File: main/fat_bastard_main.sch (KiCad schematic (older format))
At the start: 58 parts, among them J1 INPUT, J2 TO LD 12V, J3 TO LD IN, J4 TO LD GAIN, J5 TO LD OUT, J6 12V IN, J7 DI OUT, J8 FOOTSW, J9 OUTPUT, K1 FINDER-30.22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

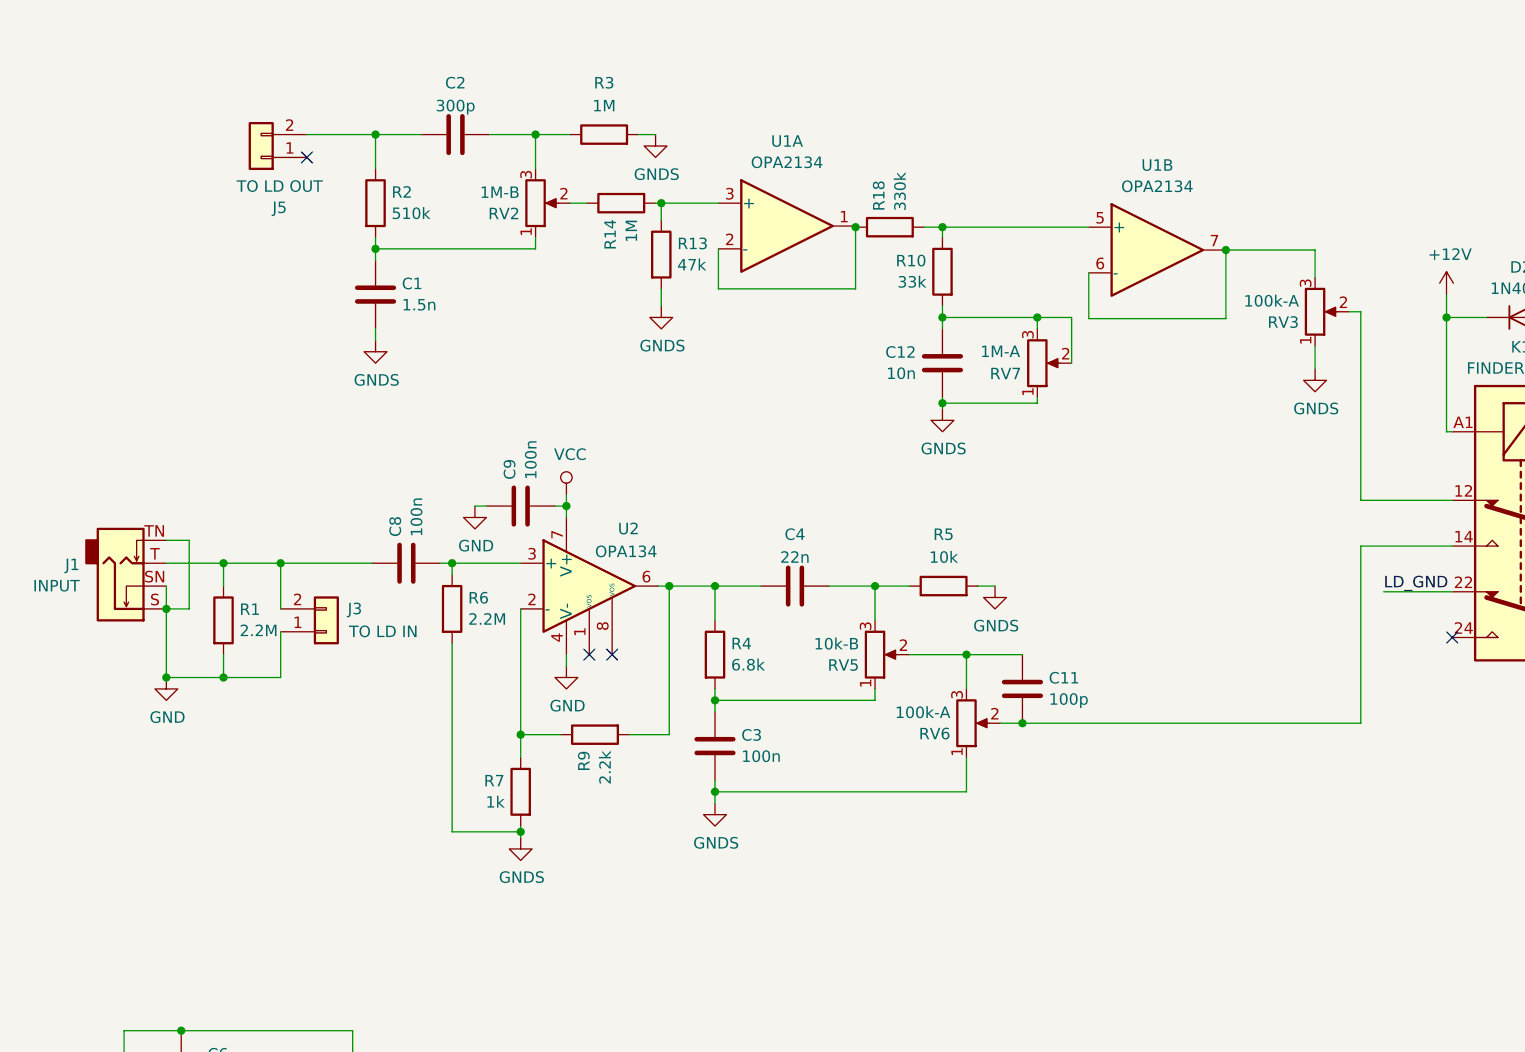
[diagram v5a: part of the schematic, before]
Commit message: [main] Fix channel switching
Due to changing the schematics layout in the previous version, default
channel is lead and is muted.

This commit restores the original layout and fixes the corresponding
traces.

Signed-off-by: Arnaud Ferraris <arnaud.ferraris@gmail.com>
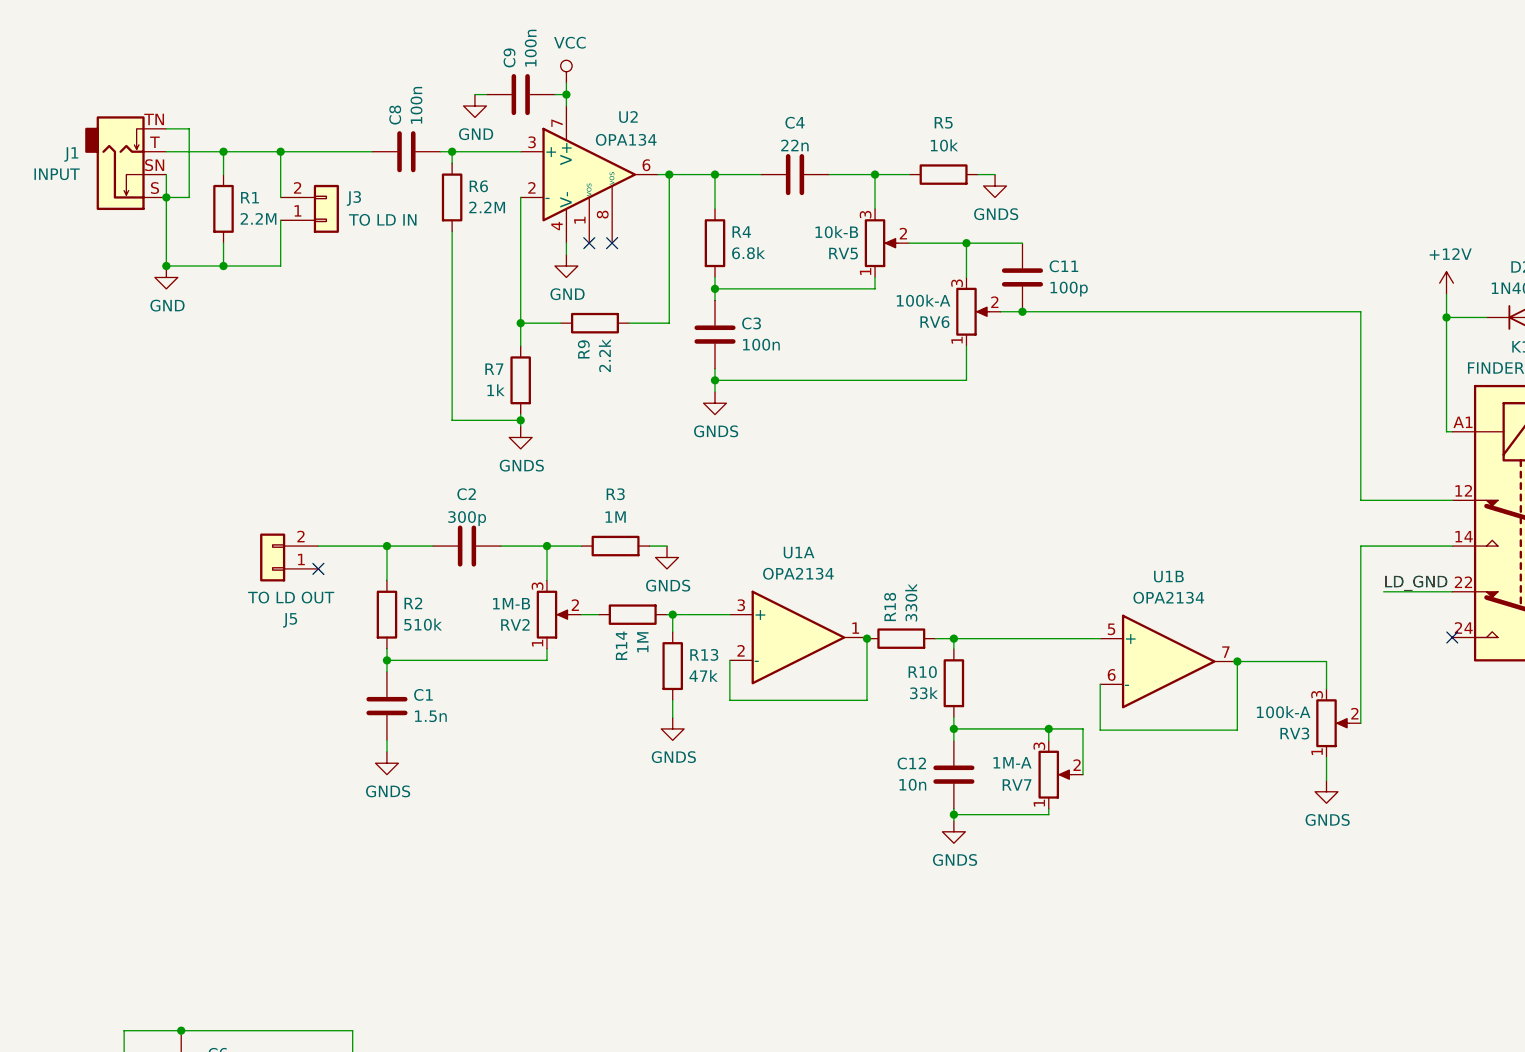
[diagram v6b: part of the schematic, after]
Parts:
- C1: MFR (none) -> WIMA; MPN (none) -> MKP2; SPN (none) -> mkp1,5nF; SPR (none) -> Musikding; SPURL (none) -> -
- C10: MFR (none) -> Nichicon; MPN (none) -> FW; SPN (none) -> 1547; SPR (none) -> Musikding; SPURL (none) -> -
- C11: MFR (none) -> -; MPN (none) -> -; SPN (none) -> glimm100pF; SPR (none) -> Musikding; SPURL (none) -> -
- C12: MFR (none) -> WIMA; MPN (none) -> MKS2D021001A00KSSD; SPN (none) -> mks10nF; SPR (none) -> Musikding; SPURL (none) -> -
- C14, C3, C5, C8, C9: MFR (none) -> WIMA; MPN (none) -> MKS2D031001A00KSSD; SPN (none) -> mks0,1uF; SPR (none) -> Musikding; SPURL (none) -> -
- C15: MFR (none) -> WIMA; MPN (none) -> MKS2C041001F00KSSD; SPN (none) -> mks1uF; SPR (none) -> Musikding; SPURL (none) -> -
- C2: MFR (none) -> -; MPN (none) -> -; SPN (none) -> glimm300pF; SPR (none) -> Musikding; SPURL (none) -> -
- C4: MFR (none) -> WIMA; MPN (none) -> MKS2C022201A00KSSD; SPN (none) -> mks22nF; SPR (none) -> Musikding; SPURL (none) -> -
- C6: MFR (none) -> -; MPN (none) -> -; SPN (none) -> glimm500pF; SPR (none) -> Musikding; SPURL (none) -> -
- C7: MFR (none) -> -; MPN (none) -> -; SPN (none) -> elko1000u16; SPR (none) -> Musikding; SPURL (none) -> -
- D1, D2: MFR (none) -> -; MPN (none) -> -; SPN (none) -> 1n4007; SPR (none) -> Musikding; SPURL (none) -> -
- D3: MFR (none) -> -; MPN (none) -> -; SPN (none) -> LED3rt; SPR (none) -> Musikding; SPURL (none) -> -
- D4: MFR (none) -> -; MPN (none) -> -; SPN (none) -> LED3gr; SPR (none) -> Musikding; SPURL (none) -> -
- J1, J9: MFR (none) -> Neutrik; MPN (none) -> NMJ4HCD2; SPN (none) -> 1845; SPR (none) -> Musikding; SPURL (none) -> -
- J2, J3, J4, J5, J7: MFR (none) -> -; MPN (none) -> -; SPN (none) -> -; SPR (none) -> -; SPURL (none) -> -
- J6, J8: MFR (none) -> Wurth; MPN (none) -> 691102710002; SPN (none) -> 826-7226; SPR (none) -> RS; SPURL (none) -> -
- K1: MFR (none) -> Omron; MPN (none) -> G5V-2; SPN (none) -> omronG5V-212; SPR (none) -> Musikding; SPURL (none) -> -
- R1, R6: MFR (none) -> -; MPN (none) -> -; SPN (none) -> 2,2Mmetall; SPR (none) -> Musikding; SPURL (none) -> -
- R10: MFR (none) -> -; MPN (none) -> -; SPN (none) -> 33kmetall; SPR (none) -> Musikding; SPURL (none) -> -
- R11, R12, R5: MFR (none) -> -; MPN (none) -> -; SPN (none) -> 10kmetall; SPR (none) -> Musikding; SPURL (none) -> -
- R13: MFR (none) -> -; MPN (none) -> -; SPN (none) -> 787; SPR (none) -> Musikding; SPURL (none) -> -
- R14, R17, R3: MFR (none) -> -; MPN (none) -> -; SPN (none) -> 1Mmetall; SPR (none) -> Musikding; SPURL (none) -> -
- R15, R21: MFR (none) -> -; MPN (none) -> -; SPN (none) -> 1k8metall; SPR (none) -> Musikding; SPURL (none) -> -
- R16: MFR (none) -> -; MPN (none) -> -; SPN (none) -> 100kmetall; SPR (none) -> Musikding; SPURL (none) -> -
- R18: MFR (none) -> -; MPN (none) -> -; SPN (none) -> 330kmetall; SPR (none) -> Musikding; SPURL (none) -> -
- R19, R7: MFR (none) -> -; MPN (none) -> -; SPN (none) -> 1kmetall; SPR (none) -> Musikding; SPURL (none) -> -
- R2: MFR (none) -> -; MPN (none) -> -; SPN (none) -> 510kmetall; SPR (none) -> Musikding; SPURL (none) -> -
- R20: MFR (none) -> -; MPN (none) -> -; SPN (none) -> 3k3metall; SPR (none) -> Musikding; SPURL (none) -> -
- R4: MFR (none) -> -; MPN (none) -> -; SPN (none) -> 6k8metall; SPR (none) -> Musikding; SPURL (none) -> -
- R8: MFR (none) -> -; MPN (none) -> -; SPN (none) -> 10Rmetall; SPR (none) -> Musikding; SPURL (none) -> -
- R9: MFR (none) -> -; MPN (none) -> -; SPN (none) -> 2k2metall; SPR (none) -> Musikding; SPURL (none) -> -
- RV1: MFR (none) -> Alpha; MPN (none) -> -; SPN (none) -> poti500klogpcb; SPR (none) -> Musikding; SPURL (none) -> -
- RV2: MFR (none) -> Alpha; MPN (none) -> -; SPN (none) -> poti1mlinpcb; SPR (none) -> Musikding; SPURL (none) -> -
- RV3, RV6: MFR (none) -> Alpha; MPN (none) -> -; SPN (none) -> poti100klogpcb; SPR (none) -> Musikding; SPURL (none) -> -
- RV5: MFR (none) -> Alpha; MPN (none) -> -; SPN (none) -> poti10klinpcb; SPR (none) -> Musikding; SPURL (none) -> -
- RV7: MFR (none) -> Alpha; MPN (none) -> -; SPN (none) -> poti1mlogpcb; SPR (none) -> Musikding; SPURL (none) -> -
- U1: MFR (none) -> Texas Instruments; MPN (none) -> OPA2134PA; SPN (none) -> 285-8069; SPR (none) -> RS; SPURL (none) -> -
- U2, U3: MFR (none) -> Texas Instruments; MPN (none) -> OPA134PA; SPN (none) -> 42469; SPR (none) -> Gotronic; SPURL (none) -> -
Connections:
- net at C11.1, RV6.2: now also K1.12; no longer K1.14
- net at RV3.2: now also K1.14; no longer K1.12
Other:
- moved on the sheet: C1, C11, C12, C2, C3, C4, C8, C9, J1, J3, J5, R1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

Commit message: Add alternate component values for guitar
In its original form, this preamp could very well be used with a guitar,
providing a rather tight and modern sound.

This patch adds alternate values, designed for use with guitar,
resulting in a warmer, fuller, stoner/rock guitar tone.

Signed-off-by: Arnaud Ferraris <arnaud.ferraris@gmail.com>
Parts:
- C11: value 100p -> not fitted
- C12: value 10n -> 15n
- C6: value 500p -> not fitted
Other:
- note added: "For guitar, use the following\nalternate component values:\nC1 1n\nC4 10n\nR5 18k\nR10 68k\nC11 1n\nC12 4.7n"
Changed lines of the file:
@@
 Sheet 1 1
 Title "Fat Bastard"
-Date "2019-04-15"
-Rev "3"
+Date "2019-05-17"
+Rev "4"
 Comp "Arnaud Ferraris (A-wai Amplification)"
 Comment1 "Licensed under CERN OHL v.1.2"
@@
 AR Path="/5C728193/5C668A4E" Ref="C?"  Part="1"
 F 0 "C6" H 1215 5148 50  0000 R CNN
-F 1 "500p" H 1215 5241 50  0000 R CNN
+F 1 "not fitted" H 1215 5241 50  0000 R CNN
 F 2 "Capacitor_THT:C_Disc_D10.5mm_W5.0mm_P5.00mm" H 1368 5045 50  0001 C CNN
 F 3 "~" H 1330 5195 50  0001 C CNN
@@
 AR Path="/5C728193/5C74E3E2" Ref="C?"  Part="1"
 F 0 "C12" H 4595 3878 50  0000 R CNN
-F 1 "10n" H 4595 3971 50  0000 R CNN
+F 1 "15n" H 4595 3971 50  0000 R CNN
 F 2 "Capacitor_THT:C_Rect_L7.2mm_W3.0mm_P5.00mm_FKS2_FKP2_MKS2_MKP2" H 4748 3775 50  0001 C CNN
 F 3 "~" H 4710 3925 50  0001 C CNN
@@
 AR Path="/5C728193/5C99F965" Ref="C?"  Part="1"
 F 0 "C11" H 4895 1703 50  0000 R CNN
-F 1 "100p" H 4895 1796 50  0000 R CNN
+F 1 "not fitted" H 4895 1796 50  0000 R CNN
 F 2 "Capacitor_THT:C_Disc_D10.5mm_W5.0mm_P5.00mm" H 5048 1600 50  0001 C CNN
 F 3 "~" H 5010 1750 50  0001 C CNN
@@
 Wire Wire Line
 	5010 1900 6490 1900
+Text Notes 9310 5945 0    50   ~ 0
+For guitar, use the following\nalternate component values:\nC1    1n\nC4    10n\nR5    18k\nR10   68k\nC11   1n\nC12   4.7n
+Wire Notes Line
+	9285 5265 10455 5265
+Wire Notes Line
+	10455 5265 10455 5980
+Wire Notes Line
+	10455 5980 9275 5980
+Wire Notes Line
+	9275 5980 9275 5265
 $EndSCHEMATC
